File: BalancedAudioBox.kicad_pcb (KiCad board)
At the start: 2 copper layers, 81 x 73 mm, 65 parts, among them IC1 TPS61252DSGT, IC2 DRV135UA_2K5, IC3 DRV135UA_2K5, J1 Conn_02x10_Odd_Even, J2 Conn_01x02, J3 XLR3_Ground, J4 XLR3_Ground, J5 Conn_01x03, J6 Conn_01x02, J8 Conn_01x03, U1 LM27762, U2 PCM5102, U3 AP1117-33

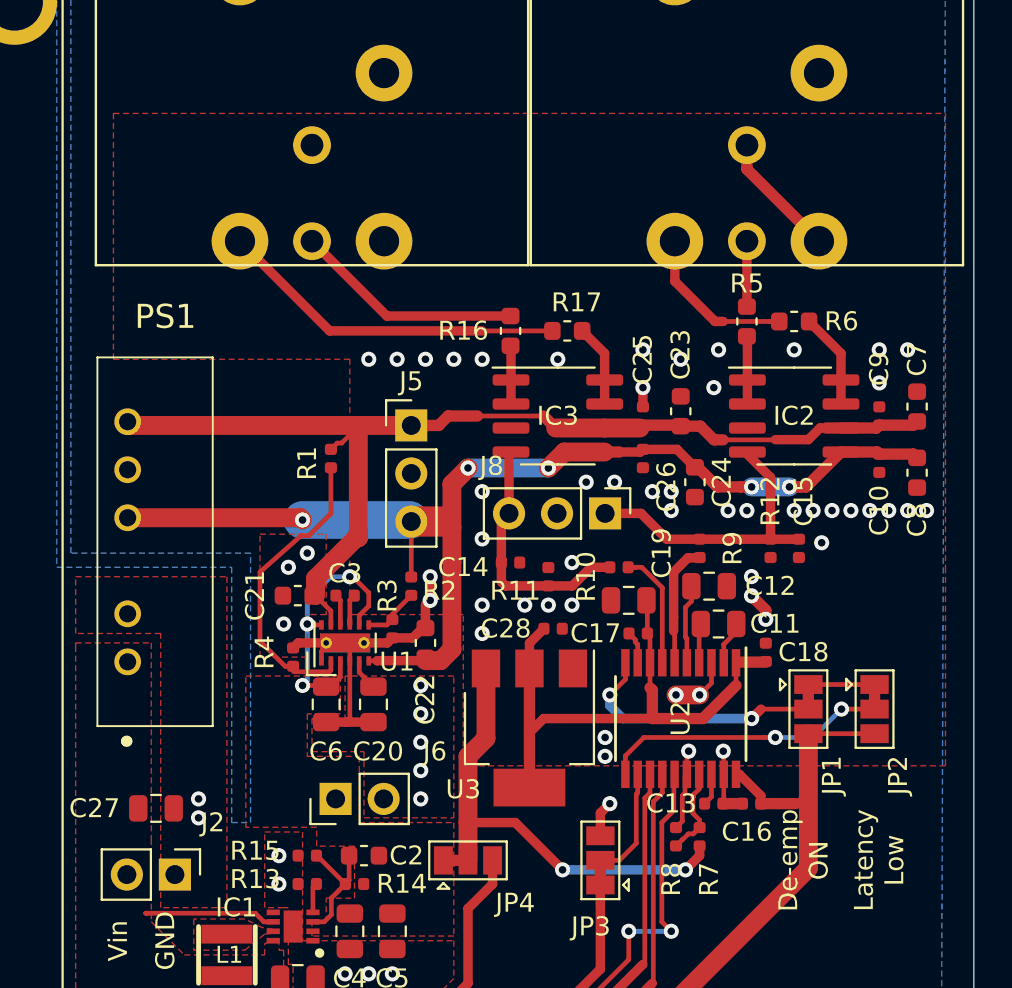
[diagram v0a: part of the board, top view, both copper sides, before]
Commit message: solder paste at 90%; changed LDO
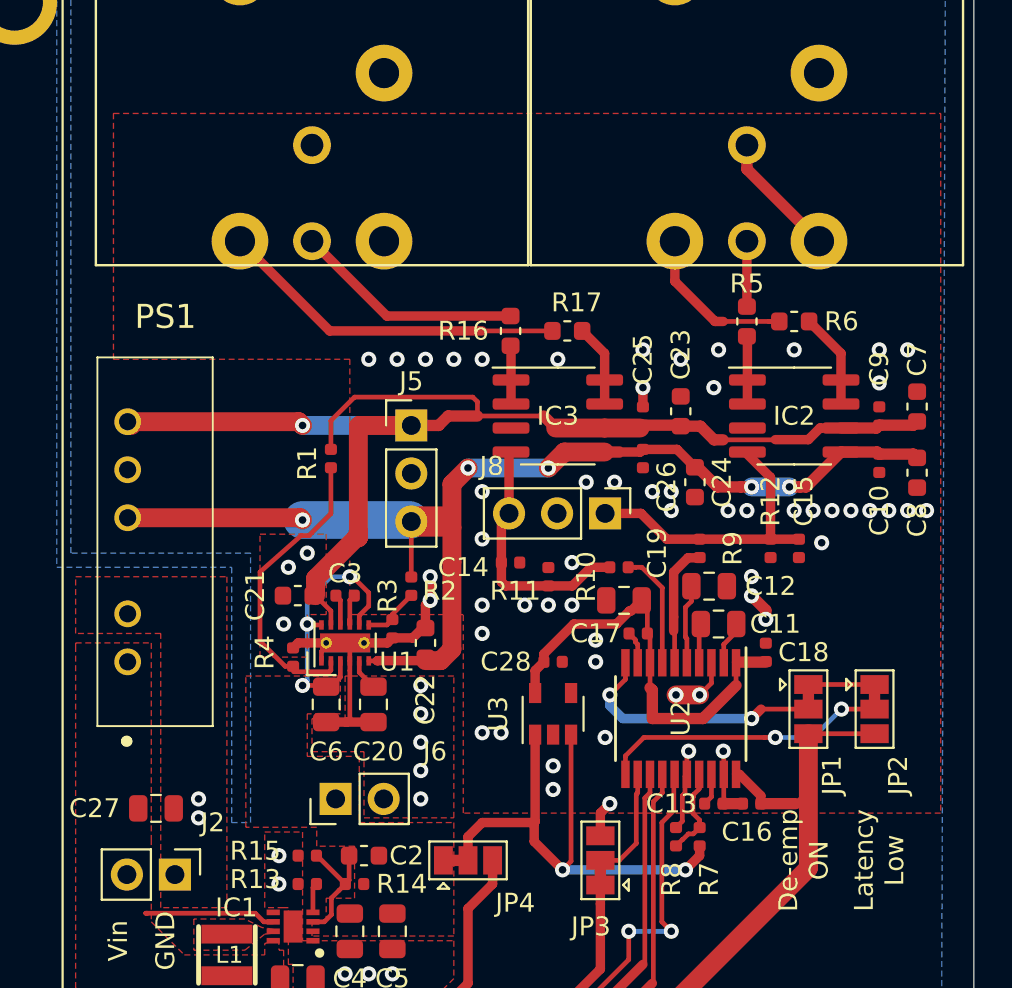
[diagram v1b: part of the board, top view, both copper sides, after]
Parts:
- U3: value AP1117-33 -> TLV75533PDBV; footprint Package_TO_SOT_SMD:SOT-223-3_TabPin2 -> Package_TO_SOT_SMD:SOT-23-5
- moved C28 1.75 mm to (168.8, 103.0)
- moved U3 1.46 mm to (168.8, 105.8), turned to 90 degrees
- moved C19 0.25 mm to (172.5, 99.8)
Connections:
- U3 pad 1: GND -> Net-(JP4-Pad2)
- U3 pad 2: +3.3VA -> GND
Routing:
- net +5V: track 57.5 -> 69.1 mm, vias 0 -> 1
- net +3.3VA: track 30.1 -> 23.2 mm
- net Net-(JP4-Pad2): track 24.7 -> 28.3 mm
- net GND: vias 68 -> 73
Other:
- rule pad_to_mask_clearance: 0.051 -> 0

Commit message: upgrade to 6
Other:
- net class Default removed
- net class Power removed
